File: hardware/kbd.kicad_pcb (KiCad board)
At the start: 2 copper layers, 139.6 x 109 mm, 99 parts, among them J1 Conn_01x12_MountingPin, J2 Conn_01x12_MountingPin, SW00 SW_Push, SW01 SW_Push, SW02 SW_Push, SW03 SW_Push, SW04 SW_Push, SW05 SW_Push, SW10 SW_Push, SW11 SW_Push, SW12 SW_Push, SW13 SW_Push, SW14 SW_Push, SW15 SW_Push, SW20 SW_Push, SW21 SW_Push, SW22 SW_Push, SW23 SW_Push, SW24 SW_Push, SW25 SW_Push, SW30 SW_Push, SW31 SW_Push, SW32 SW_Push, SW33 SW_Push, SW34 SW_Push, SW35 SW_Push, SW36 SW_Push, SW37 SW_Push, U1 CH582, U2 74HC165, U4 74HC165

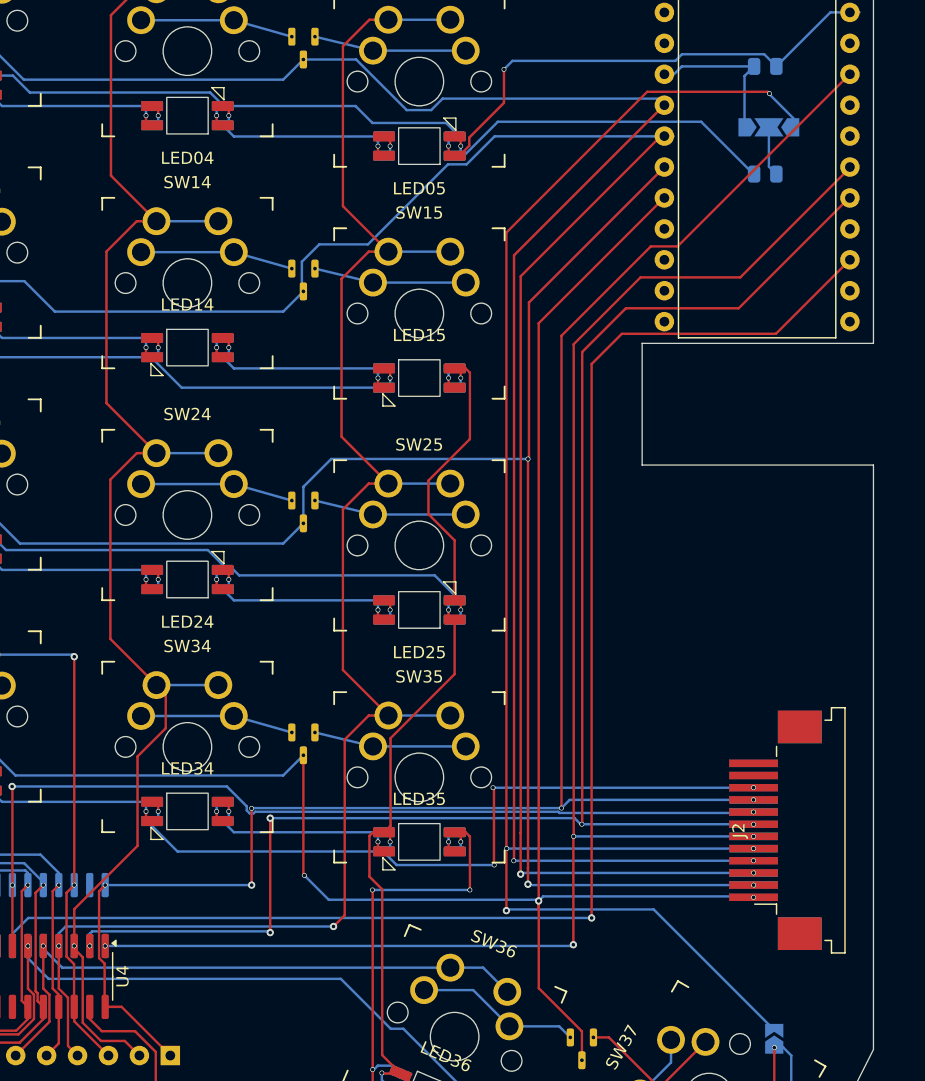
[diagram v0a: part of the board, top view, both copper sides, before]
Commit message: Fixed row2 and row3 pin connections and added gerber files
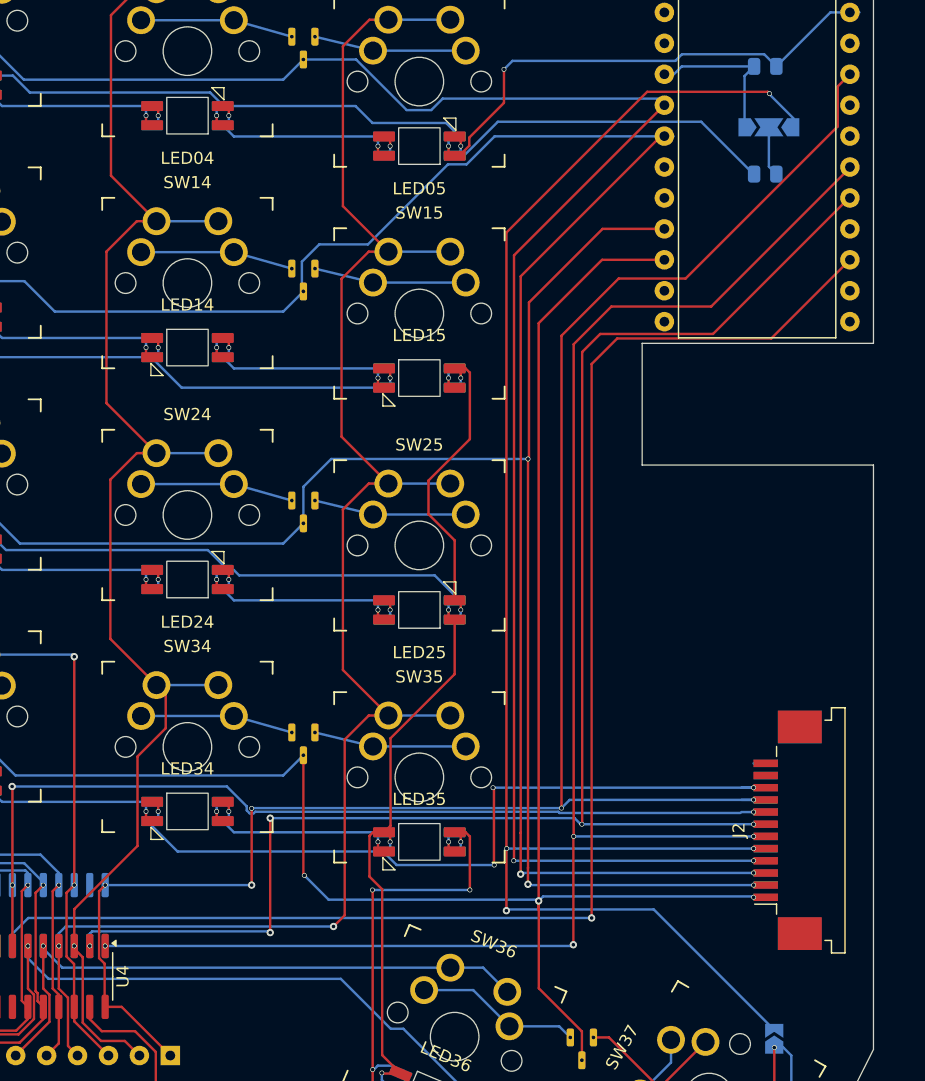
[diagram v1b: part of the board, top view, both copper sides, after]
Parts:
- removed ? (x24): , 
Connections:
- U1 pad 10: unconnected-(U1-B4-Pad10) -> ROW3
- U1 pad 7: ROW2 -> unconnected-(U1-B11-Pad7)
- U1 pad 8: ROW3 -> unconnected-(U1-B10-Pad8)
- U1 pad 9: unconnected-(U1-B7-Pad9) -> ROW2
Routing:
- net ROW2: track 192.8 -> 189.7 mm
- net ROW3: track 212.4 -> 210.3 mm
- net +3V3: track 151.6 -> 153.5 mm
- net SCS: track 134.4 -> 133.4 mm
- net SCK0: track 134.2 -> 133.2 mm
- net ROW1: track 209.9 -> 208.9 mm
- net ROW0: track 207.2 -> 206.2 mm
- net LED_R: track 135.2 -> 134.2 mm

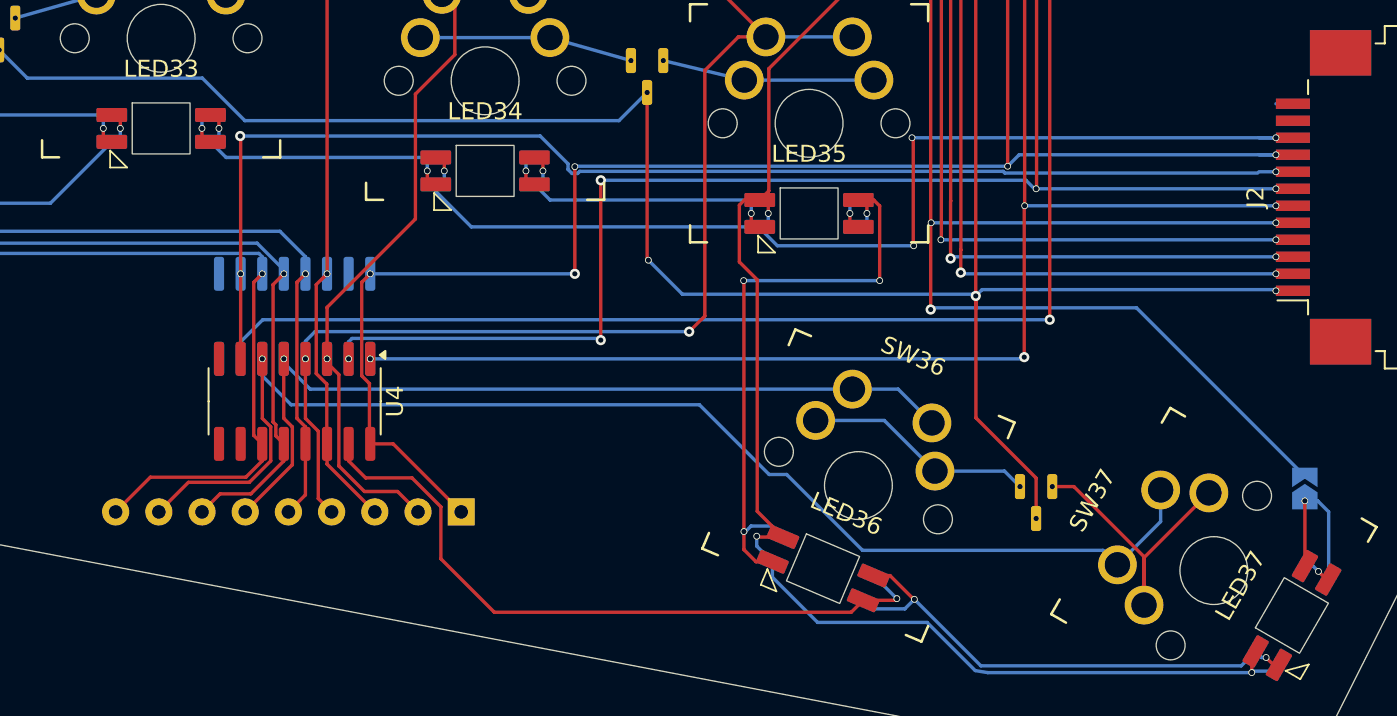
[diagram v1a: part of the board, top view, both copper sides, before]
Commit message: Replaced SIP resistor with 0602x8
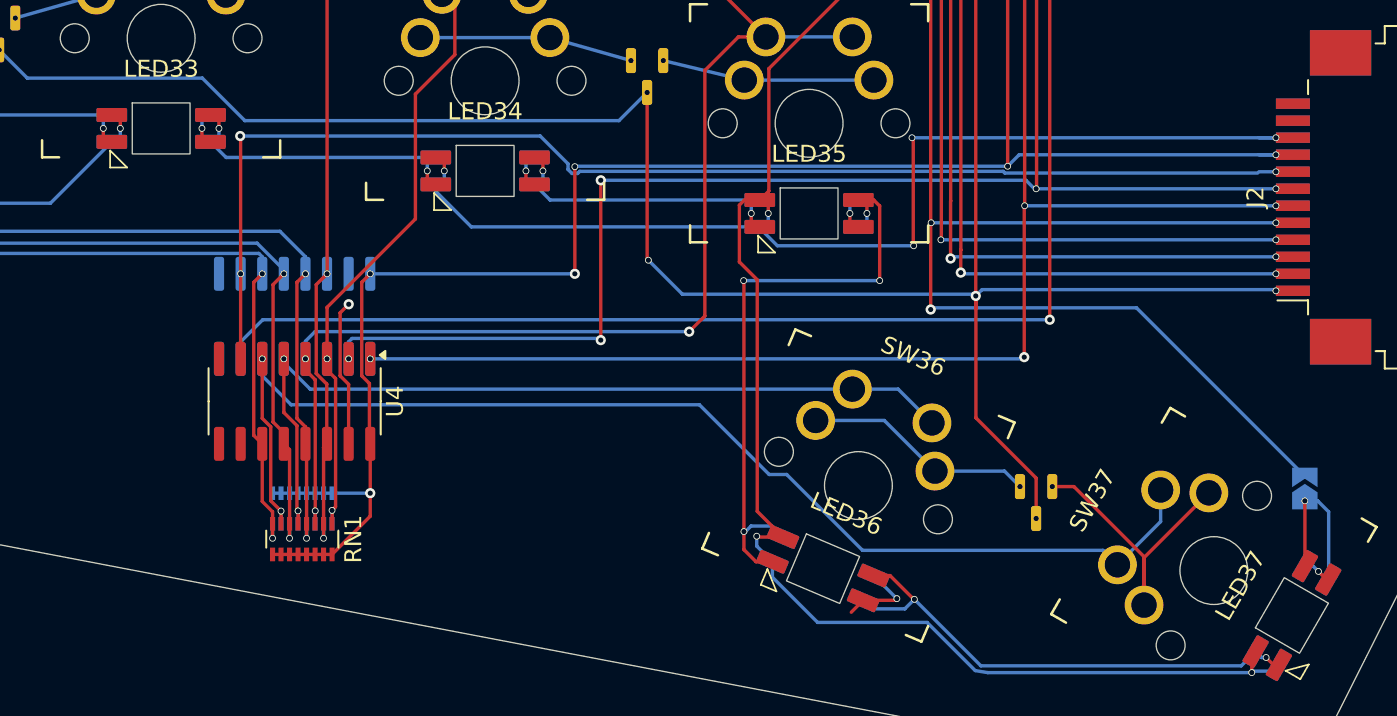
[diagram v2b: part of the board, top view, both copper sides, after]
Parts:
- added RN2: R_Pack08, Resistor_SMD:R_Array_Convex_8x0602, B.Cu at (125.5, 133.3)
- RN1: value 10kOhm -> R_Pack08; footprint Resistor_THT:R_Array_SIP9 -> Resistor_SMD:R_Array_Convex_8x0602; moved to F.Cu
- moved RN1 9.48 mm to (125.5, 135.1), turned to -90 degrees
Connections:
- RN1 pad 1: +3V3 -> COL4
- RN1 pad 2: COL4 -> COL3
- RN1 pad 3: COL3 -> COL5
- RN1 pad 4: COL5 -> COL2
- RN1 pad 5: COL2 -> COL6
- RN1 pad 6: COL6 -> COL1
- RN1 pad 7: COL1 -> COL7
- RN1 pad 8: COL7 -> COL0
- RN1 pad 9: COL0 -> +3V3
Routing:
- net GND: track 81.5 -> 53.1 mm, vias 26 -> 27
- net +3V3: track 153.5 -> 163.2 mm, vias 5 -> 6
- net COL0: track 183.4 -> 179.1 mm, vias 2 -> 3
- net COL7: track 75.4 -> 72.2 mm, vias 1 -> 2
- net COL2: track 144.0 -> 146.0 mm, vias 2 -> 3
- net COL4: track 126.9 -> 125.6 mm, vias 1 -> 2
- net COL3: track 131.6 -> 132.9 mm, vias 2 -> 3
- net COL5: track 143.3 -> 144.3 mm, vias 2 -> 3
- net COL1: track 152.2 -> 151.7 mm, vias 2 -> 3
- net COL6: track 49.9 -> 50.4 mm, vias 1 -> 2
